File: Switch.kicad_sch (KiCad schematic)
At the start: 0 parts

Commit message: progress on switch sheet
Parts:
- added C501: 1uF, Capacitor_SMD:C_0603_1608Metric_Pad1.08x0.95mm_HandSolder, symbol Device:C_Small
- added Q501, Q502, Q503: ~, Package_TO_SOT_SMD:TO-252-2, symbol Transistor_FET:RS9N50D
- added R501: 1mR, symbol Device:R_Small
- added R502, R509, R510, R511, R512, R515: 10kR, symbol Device:R_Small
- added R503, R504, R505, R506, R507, R508: 0R, symbol Device:R_Small
- added R513, R514, R516: 10R, symbol Device:R_Small
- added U501: INA226, Package_SO:VSSOP-10_3x3mm_P0.5mm, symbol Sensor_Energy:INA226
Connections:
- net EN: now also Q503.2 (D)
- net VIN: now also R501.1, U501.10 (Vin+), U501.8 (Vbus)
- net VOUT: now also Q501.3 (S), Q502.3 (S)
- new net: R504.2, R507.2, R508.2, U501.1 (A1)
- new net: R503.2, R505.2, R506.2, U501.2 (A0)
- new net: Q501.2 (D), Q502.2 (D), R501.2, U501.9 (Vin-)
- new net: Q502.1 (G), R509.2, R513.1
- new net: Q501.1 (G), R502.2, R514.1
- new net: Q503.1 (G), R515.2, R516.1
- new net: Q503.3 (S), R513.2, R514.2
- new net +3.3V: R510.1, R511.2, R512.1
- new net +5V: C501.1, U501.6 (VS)
- new net GND: C501.2, R502.1, R503.1, R504.1, R509.1, R515.1, U501.7 (GND)
- new net SCL: R506.1, R508.1, R510.2, U501.5 (SCL)
- new net SDA: R505.1, R507.1, R511.1, U501.4 (SDA)
- new net ~{ALERT}: R512.2, R516.2, U501.3 (~{Alert})

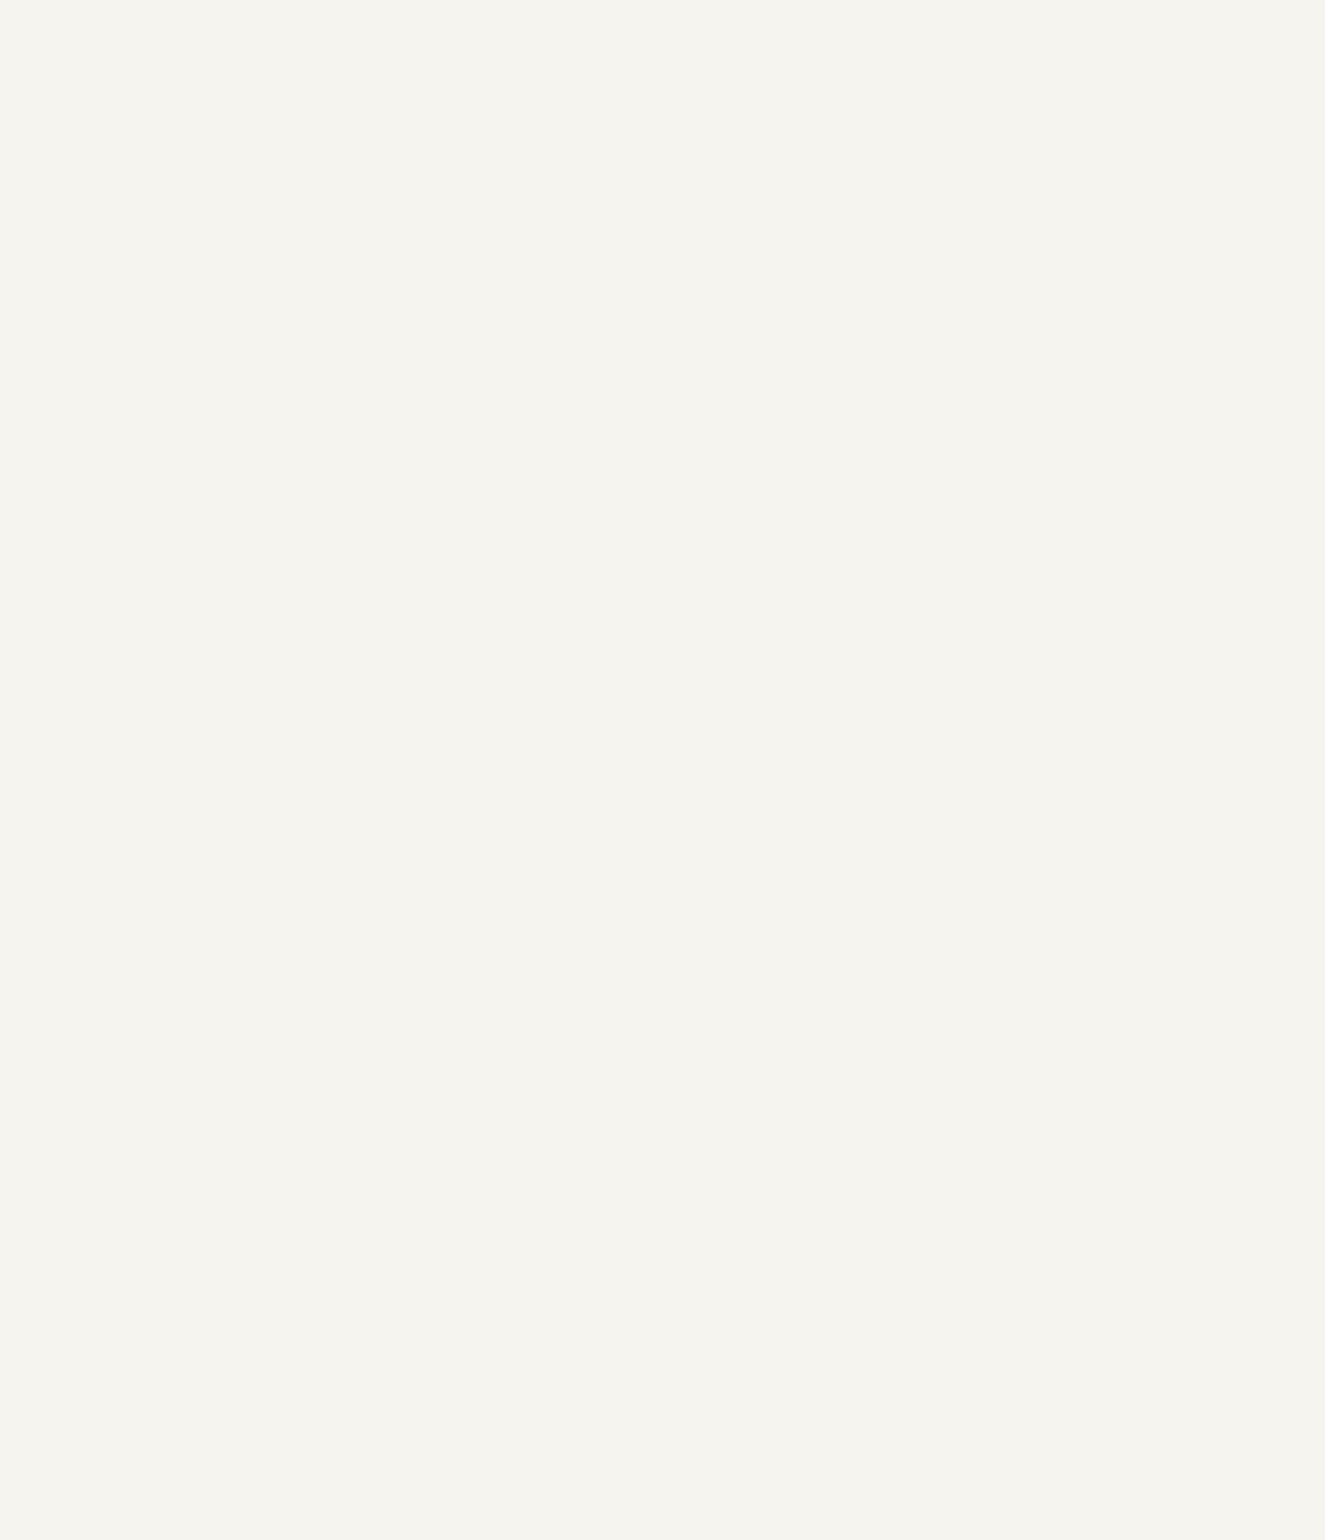
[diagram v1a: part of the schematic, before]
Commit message: added possible parts to switch sheet
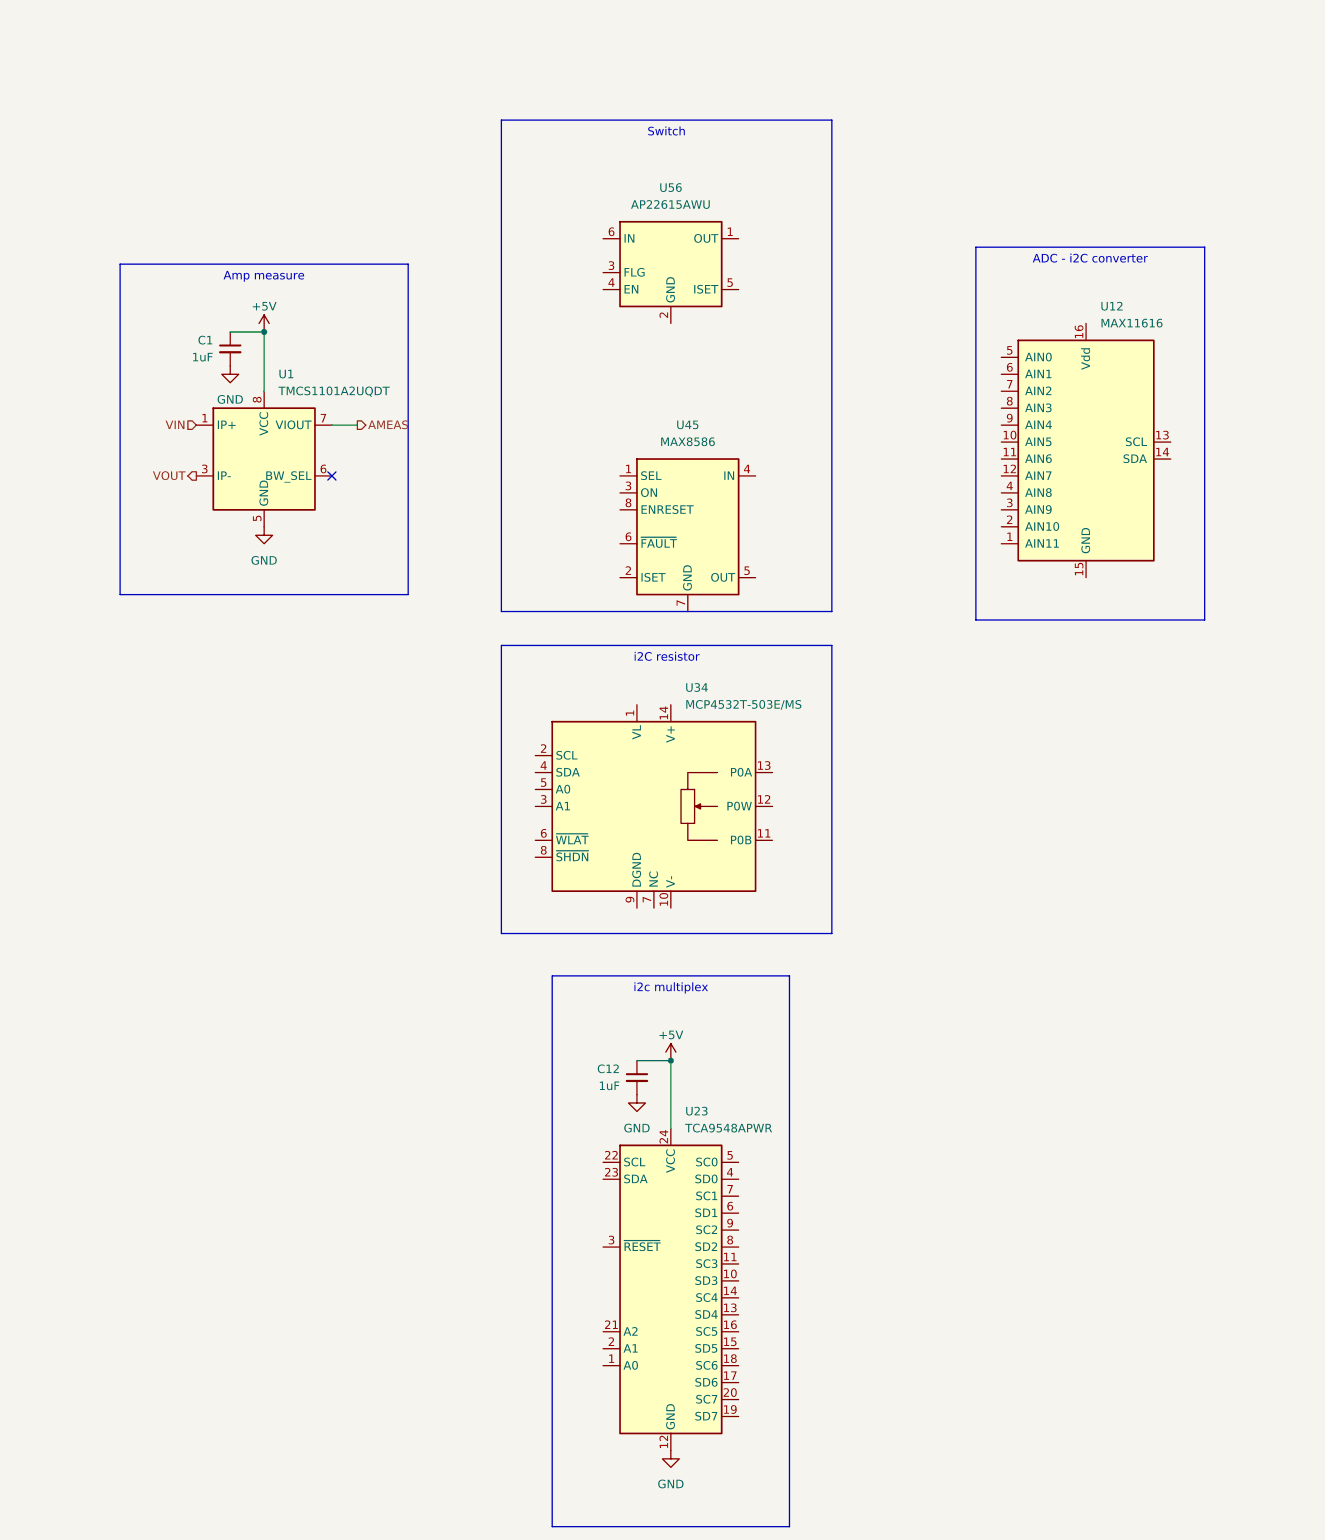
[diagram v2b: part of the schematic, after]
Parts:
- added C1, C12: 1uF, Capacitor_SMD:C_0603_1608Metric_Pad1.08x0.95mm_HandSolder, symbol Device:C_Small
- added U1: TMCS1101A2UQDT, Package_SO:SOIC-8_3.9x4.9mm_P1.27mm, symbol Sensor_Current:ACS723xLCTR-40AB
- added U12: MAX11616, Package_SO:QSOP-16_3.9x4.9mm_P0.635mm, symbol Analog_ADC:MAX11616
- added U23: TCA9548APWR, Package_SO:TSSOP-24_4.4x7.8mm_P0.65mm, symbol Interface_Expansion:TCA9548APWR
- added U34: MCP4532T-503E/MS, Package_SO:TSSOP-14_4.4x5mm_P0.65mm, symbol Potentiometer_Digital:MCP45HV31-ST
- added U45: MAX8586, Package_DFN_QFN:DFN-8-1EP_3x3mm_P0.65mm_EP1.55x2.4mm, symbol Power_Management:MAX8586
- added U56: AP22615AWU, Package_TO_SOT_SMD:SOT-23-6, symbol Regulator_Linear:AP22615AWU
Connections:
- net +5V: now also C1.1, C12.1, U1.8 (VCC), U23.24 (VCC)
- net AMEAS: now also U1.7 (VIOUT)
- net GND: now also C1.2, C12.2, U1.5 (GND), U23.12 (GND)
- net VIN: now also U1.1 (IP+), U1.2 (IP+)
- net VOUT: now also U1.3 (IP-), U1.4 (IP-)
- new net: U45.7 (GND), U45.9 (GND)
- no-connect marks 0 -> 1

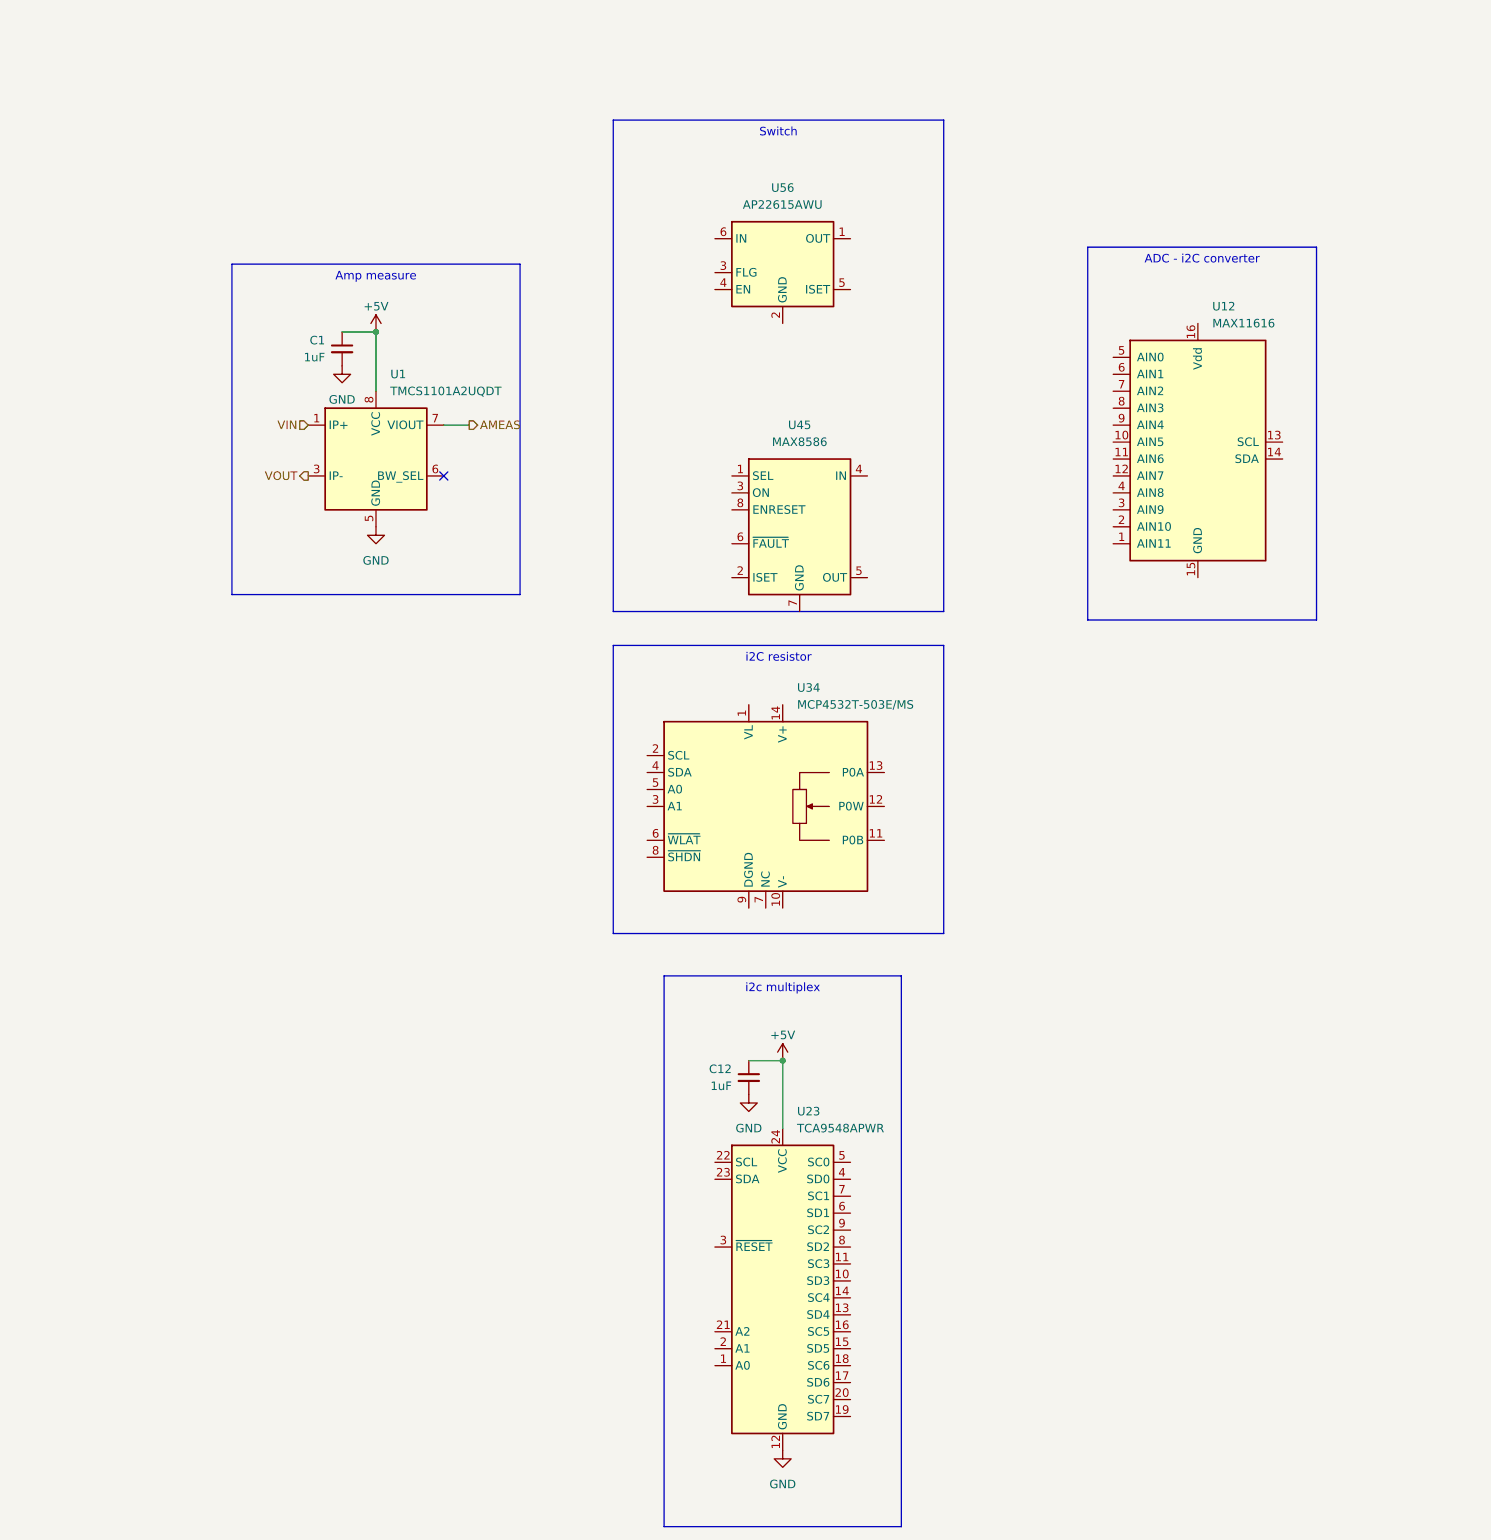
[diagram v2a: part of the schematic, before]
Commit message: specified parts and connection, updated notes
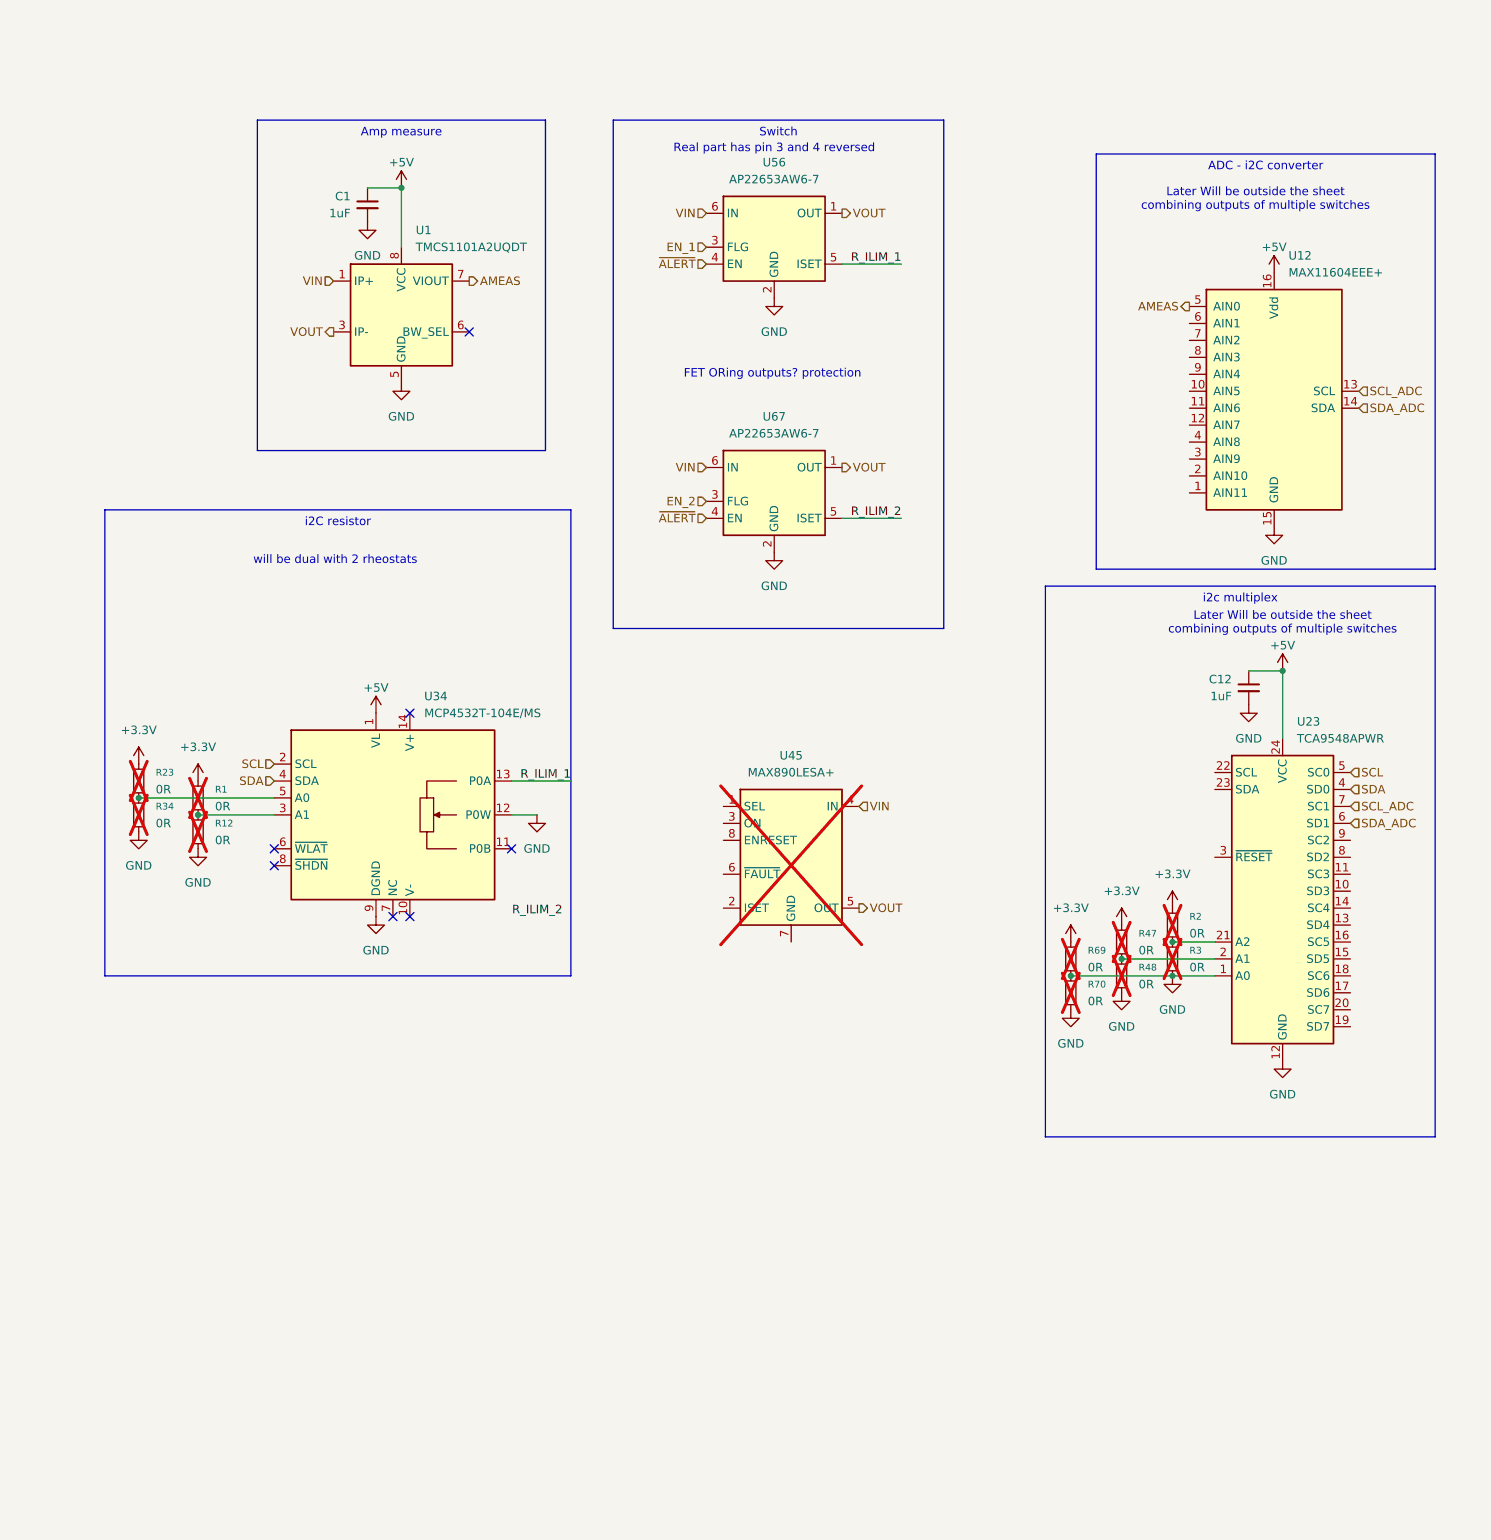
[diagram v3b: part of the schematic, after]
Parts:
- added R1, R12, R2, R23, R3, R34, R47, R48, R69, R70: 0R, symbol Device:R_Small
- added U67: AP22653AW6-7, Package_TO_SOT_SMD:SOT-23-6, symbol Regulator_Linear:AP22615AWU
- U12: value MAX11616 -> MAX11604EEE+
- U34: value MCP4532T-503E/MS -> MCP4532T-104E/MS
- U45: value MAX8586 -> MAX890LESA+; now not fitted
- U56: value AP22615AWU -> AP22653AW6-7
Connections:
- net +3.3V: now also R1.2, R2.2, R23.2, R47.2, R69.2
- net +5V: now also U12.16 (Vdd), U34.1 (VL)
- net AMEAS: now also U12.5 (AIN0)
- net GND: now also U12.15 (GND), U23.1 (A0), U34.12 (P0W), U34.9 (DGND), U56.2 (GND), R12.1, R3.1, R34.1, R48.1, R69.1, R70.1, R70.2, U67.2 (GND)
- net SCL: now also U23.5 (SC0), U34.2 (SCL)
- net SDA: now also U23.4 (SD0), U34.4 (SDA)
- net VIN: now also U45.4 (IN), U56.6 (IN), U67.6 (IN)
- net VOUT: now also U45.5 (OUT), U56.1 (OUT), U67.1 (OUT)
- net ~{ALERT}: now also U56.4 (EN), U67.4 (EN)
- net SCL_ADC: now reaches U12.13 (SCL)
- net SCL_ADC: now also U23.7 (SC1)
- net SDA_ADC: now reaches U12.14 (SDA)
- net SDA_ADC: now also U23.6 (SD1)
- net EN_1: now reaches U56.3 (FLG)
- net R_ILIM_1: now reaches U56.5 (ISET)
- net R_ILIM_1: now also U34.13 (P0A)
- net at U34.3 (A1): now also R1.1, R12.2
- net at U34.5 (A0): now also R23.1, R34.2
- net at U23.2 (A1): now also R47.1, R48.2
- net at U23.21 (A2): now also R2.1, R3.2
- new net EN_2: U67.3 (FLG)
- new net R_ILIM_2: U67.5 (ISET)
- no-connect marks 1 -> 7
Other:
- note added: "FET ORing outputs? protection"
- note added: "Later Will be outside the sheet combining outputs of multiple switches"
- note added: "Real part has pin 3 and 4 reversed"
- note added: "will be dual with 2 rheostats"
- moved on the sheet: C1, C12, U1, U12, U23, U34, U56
